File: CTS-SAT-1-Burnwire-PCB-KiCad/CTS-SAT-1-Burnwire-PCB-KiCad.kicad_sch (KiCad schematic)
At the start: 16 parts, among them J1 feather long, J2 feather short, U1 ADP2303ARDZ

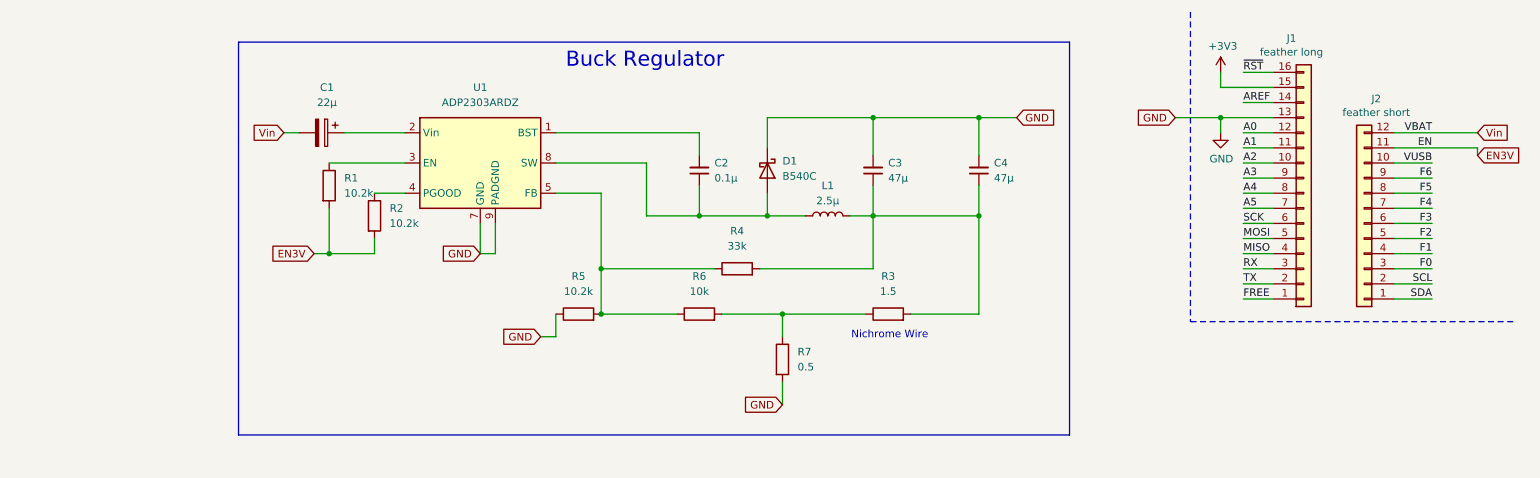
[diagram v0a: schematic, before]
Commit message: Low Side Switch Burnwire Design
Added 350mA current limiting low side switch
Added footprints for two thru-hole and two SMD burn resistors
Added Picoblade connectors
Added LEDs and test switches
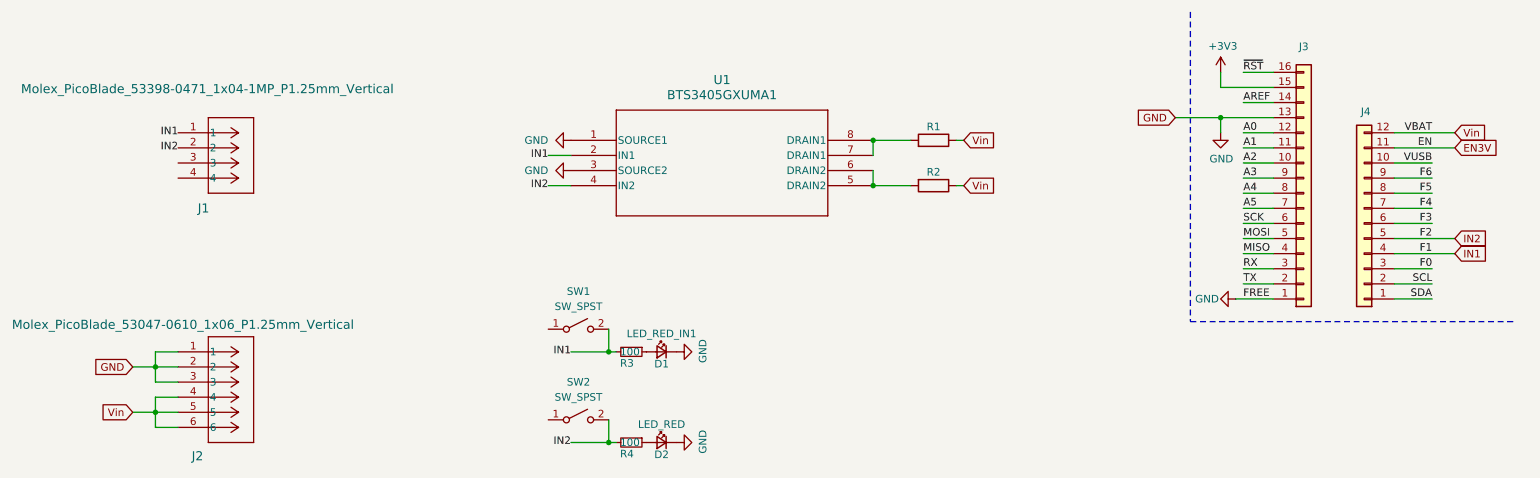
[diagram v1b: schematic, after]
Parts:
- removed C1: 22µ, Capacitor_Tantalum_SMD:CP_EIA-1608-08_AVX-J, symbol Device:C_Polarized
- removed C2: 0.1µ, Capacitor_SMD:C_0201_0603Metric, symbol Device:C_Small
- removed C3, C4: 47µ, Capacitor_SMD:C_0201_0603Metric, symbol Device:C_Small
- removed D1: B540C, Diode_SMD:D_01005_0402Metric, symbol Device:D_Schottky
- removed L1: 2.5µ, Inductor_SMD:L_0201_0603Metric, symbol Device:L
- removed R1, R2, R5: 10.2k, Resistor_SMD:R_0201_0603Metric, symbol Device:R
- removed R3: 1.5, Resistor_SMD:R_0201_0603Metric, symbol Device:R
- removed R4: 33k, Resistor_SMD:R_0201_0603Metric, symbol Device:R
- removed R6: 10k, Resistor_SMD:R_0201_0603Metric, symbol Device:R
- removed R7: 0.5, Resistor_SMD:R_0201_0603Metric, symbol Device:R
- removed U1: ADP2303ARDZ, Package_SO:SOIC-8-1EP_3.9x4.9mm_P1.27mm_EP2.29x3mm, symbol Regulator_Switching:ADP2303ARDZ
- added D1: LED_RED_IN1, LED_SMD:LED_0805_2012Metric, symbol Library:LED_Small
- added D2: LED_RED, LED_SMD:LED_0805_2012Metric, symbol Library:LED_Small
- added J1: Molex_PicoBlade_53398-0471_1x04-1MP_P1.25mm_Verti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, Connector_Molex:Molex_PicoBlade_53261-0471_1x04-1MP_P1.25mm_Horizontal, symbol Library:533980471
- added J2: Molex_PicoBlade_53047-0610_1x06_P1.25mm_Vertical, Connector_Molex:Molex_PicoBlade_53047-0610_1x06_P1.25mm_Vertical, symbol Library:530470660
- added R1: R_2512_6332Metric, Resistor_SMD:R_2512_6332Metric, symbol Library:R
- added R2: R, Resistor_SMD:R_2512_6332Metric, symbol Library:R
- added R3, R4: 100, Resistor_SMD:R_0603_1608Metric, symbol Library:R_Small
- added SW1, SW2: SW_SPST, symbol Library:SW_SPST
- added U1: BTS3405GXUMA1, footprints2:PG-DSO-8-25_INF, symbol Library:BTS3405GXUMA1
- J3: renamed from J1; symbol Connector_Generic:Conn_01x16 -> Library:Conn_01x16
- J4: renamed from J2; symbol Connector_Generic:Conn_01x12 -> Library:Conn_01x12
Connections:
- net FREE is gone; now on net GND: J3.1 (Pin_1)
- net GND: now also D1.1 (K), D2.1 (K), J2.1, J2.2, J2.3, U1.1 (SOURCE1), U1.3 (SOURCE2)
- net Vin: now also J2.4, J2.5, J2.6, R1.1, R2.1
- net F1 renamed IN1
- net IN1: now also J1.1, R3.2, SW1.2 (B), U1.2 (IN1)
- net F2 renamed IN2
- net IN2: now also J1.2, R4.2, SW2.2 (B), U1.4 (IN2)
- new net: D1.2 (A), R3.1
- new net: R1.2, U1.7 (DRAIN1), U1.8 (DRAIN1)
- new net: D2.2 (A), R4.1
- new net: R2.2, U1.5 (DRAIN2), U1.6 (DRAIN2)
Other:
- note removed: "Buck Regulator"
- note removed: "Nichrome Wire"
